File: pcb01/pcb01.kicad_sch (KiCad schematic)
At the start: 26 parts, among them J1 DIN41612_02x32_AC, J2 Conn_01x08_Socket, J3 Conn_01x16_Socket, SW1 SW_Push, U1 W65C02SxP, U2 HM62256BLP, U3 27C512, U4 PAL20RS10, U5 74LS138, U6 74HCT574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

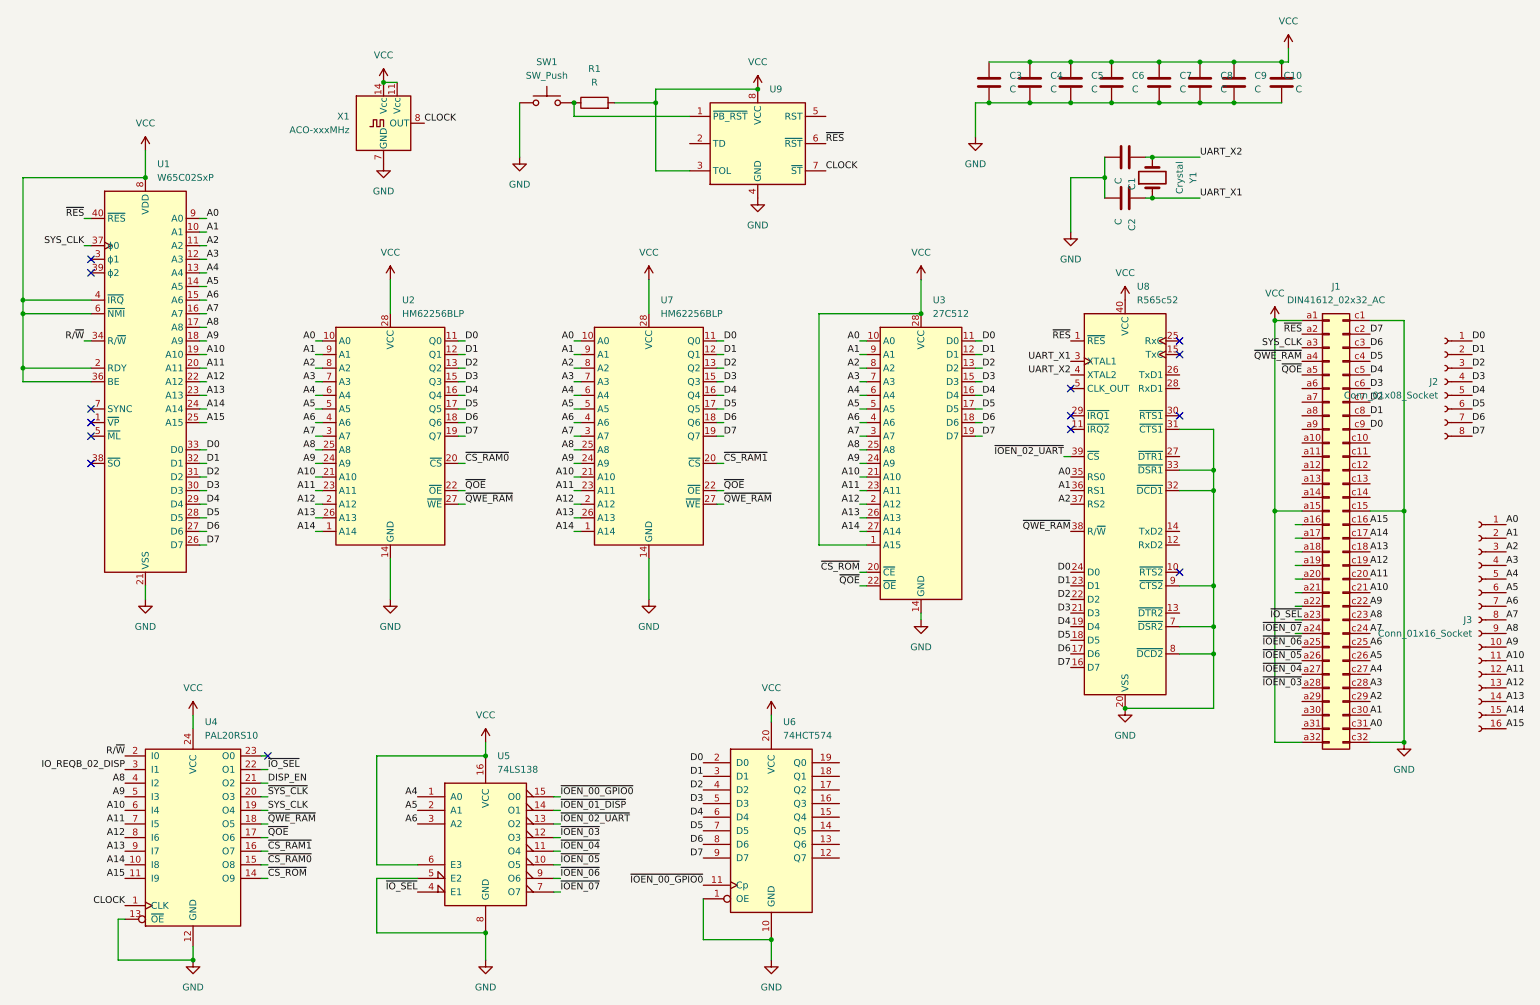
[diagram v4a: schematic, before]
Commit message: fix some schematic bugs
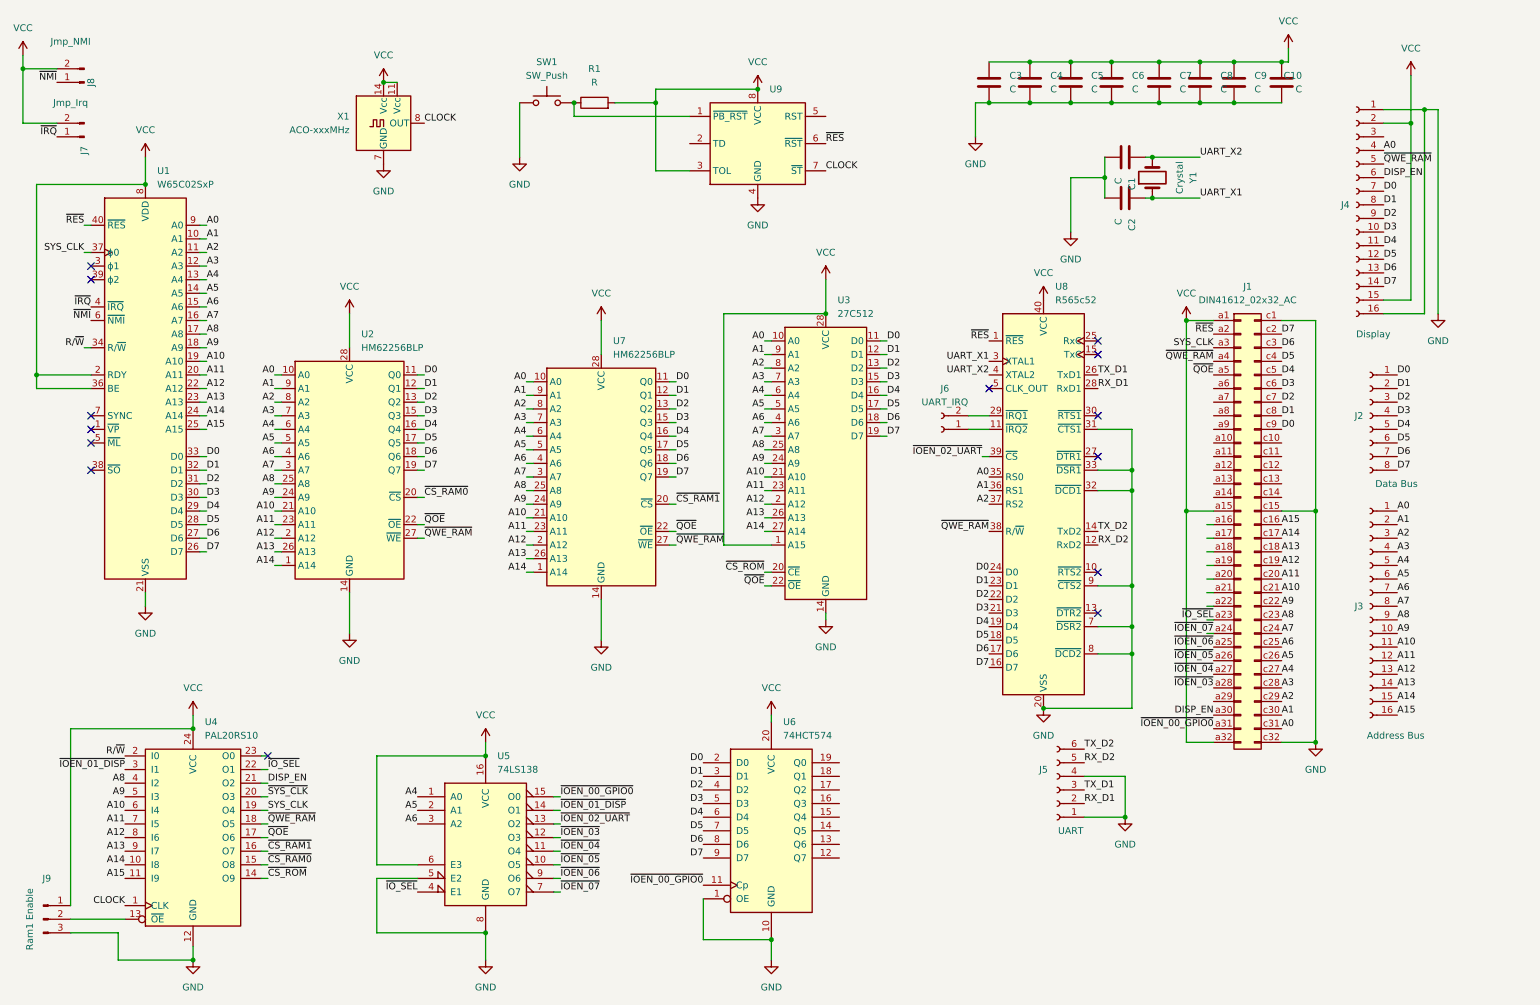
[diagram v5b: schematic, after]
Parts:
- added J4: Display, Connector_PinSocket_2.54mm:PinSocket_1x16_P2.54mm_Vertical, symbol Connector:Conn_01x16_Socket
- added J5: UART, Connector_PinSocket_2.54mm:PinSocket_1x06_P2.54mm_Vertical, symbol Connector:Conn_01x06_Socket
- added J6: UART_IRQ, Connector_PinHeader_2.00mm:PinHeader_1x02_P2.00mm_Vertical, symbol Connector:Conn_01x02_Socket
- added J7: Jmp_Irq, Connector_PinHeader_2.00mm:PinHeader_1x02_P2.00mm_Vertical, symbol Connector:Conn_01x02_Pin
- added J8: Jmp_NMI, Connector_PinHeader_2.00mm:PinHeader_1x02_P2.00mm_Vertical, symbol Connector:Conn_01x02_Pin
- added J9: Ram1 Enable, Connector_PinHeader_2.54mm:PinHeader_1x03_P2.54mm_Vertical, symbol Connector:Conn_01x03_Pin
- J2: value Conn_01x08_Socket -> Data Bus
- J3: value Conn_01x16_Socket -> Address Bus
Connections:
- net IO_REQB_02_DISP is gone; now on net ~{IOEN_01_DISP}: U4.3 (I1)
- net A0: now also J4.4 (Pin_4)
- net D0: now also J4.7 (Pin_7)
- net D1: now also J4.8 (Pin_8)
- net D2: now also J4.9 (Pin_9)
- net D3: now also J4.10 (Pin_10)
- net D4: now also J4.11 (Pin_11)
- net D5: now also J4.12 (Pin_12)
- net D6: now also J4.13 (Pin_13)
- net D7: now also J4.14 (Pin_14)
- net DISP_EN: now also J1.a30 (Pin_a30), J4.6 (Pin_6)
- net GND: now also J4.1 (Pin_1), J4.16 (Pin_16), J5.1 (Pin_1), J5.4 (Pin_4), J9.3 (Pin_3); no longer U4.13 (~{OE})
- net VCC: now also J4.15 (Pin_15), J4.2 (Pin_2), J7.2 (Pin_2), J8.2 (Pin_2), J9.1 (Pin_1); no longer U1.4 (~{IRQ}), U1.6 (~{NMI})
- net ~{IOEN_00_GPIO0}: now also J1.a31 (Pin_a31)
- net ~{QWE_RAM}: now also J4.5 (Pin_5)
- net at U8.11 (~{IRQ2}): now also J6.1 (Pin_1)
- net RX_D2: now reaches U8.12 (RxD2)
- net RX_D2: now also J5.5 (Pin_5)
- net TX_D2: now reaches U8.14 (TxD2)
- net TX_D2: now also J5.6 (Pin_6)
- net TX_D1: now reaches U8.26 (TxD1)
- net TX_D1: now also J5.3 (Pin_3)
- net RX_D1: now reaches U8.28 (RxD1)
- net RX_D1: now also J5.2 (Pin_2)
- net at U8.29 (~{IRQ1}): now also J6.2 (Pin_2)
- new net: J9.2 (Pin_2), U4.13 (~{OE})
- new net ~{IRQ}: J7.1 (Pin_1), U1.4 (~{IRQ})
- new net ~{NMI}: J8.1 (Pin_1), U1.6 (~{NMI})
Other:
- moved on the sheet: J1, J2, J3, U1, U2, U3, U7, U8

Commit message: pcb refinement
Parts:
- added C11: C_Polarized, Capacitor_THT:CP_Radial_D8.0mm_P5.00mm, symbol Device:C_Polarized
- added C12, C13: C_Polarized, Capacitor_THT:CP_Radial_D5.0mm_P2.50mm, symbol Device:C_Polarized
- added J10: Conn_01x02_Socket, Connector_PinSocket_2.54mm:PinSocket_1x02_P2.54mm_Vertical, symbol Connector:Conn_01x02_Socket
- U1, U8: footprint Package_DIP:DIP-40_W15.24mm -> Package_DIP:DIP-40_W15.24mm_Socket
- U3: footprint Package_DIP:DIP-28_W15.24mm -> Package_DIP:DIP-28_W15.24mm_Socket
- U4: footprint Package_DIP:DIP-24_W7.62mm -> Package_DIP:DIP-24_W7.62mm_Socket
- U5: footprint Package_DIP:DIP-16_W7.62mm -> Package_DIP:DIP-16_W7.62mm_Socket
- U6: footprint Package_DIP:DIP-20_W7.62mm -> Package_DIP:DIP-20_W7.62mm_Socket
- U9: value ~ -> MAX1232
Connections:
- net GND: now also C11.2, C12.2, C13.2, J10.2 (Pin_2)
- net VCC: now also C11.1, C12.1, C13.1, J10.1 (Pin_1)
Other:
- moved on the sheet: C10, C3, C4, C5, C6, C7, C8, C9

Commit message: connect GPIO0
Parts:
- added J11: Conn_01x09, Connector_PinSocket_2.54mm:PinSocket_1x09_P2.54mm_Vertical, symbol Connector_Generic:Conn_01x09
- added RV1: R_LCD_BIAS, Potentiometer_THT:Potentiometer_Vishay_T73YP_Vertical, symbol Device:R_Potentiometer_Small
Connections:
- net GND: now also J11.1 (Pin_1), RV1.3
- net VCC: now also RV1.1
- net ~{SYS_CLK}: now also J1.a16 (Pin_a16)
- net LCD_BIAS: now reaches J4.3 (Pin_3)
- net LCD_BIAS: now also RV1.2
- net at U6.12 (Q7): now also J11.9 (Pin_9)
- net at U6.13 (Q6): now also J11.8 (Pin_8)
- net at U6.14 (Q5): now also J11.7 (Pin_7)
- net at U6.15 (Q4): now also J11.6 (Pin_6)
- net at U6.16 (Q3): now also J11.5 (Pin_5)
- net at U6.17 (Q2): now also J11.4 (Pin_4)
- net at U6.18 (Q1): now also J11.3 (Pin_3)
- net at U6.19 (Q0): now also J11.2 (Pin_2)
- no-connect marks 14 -> 37

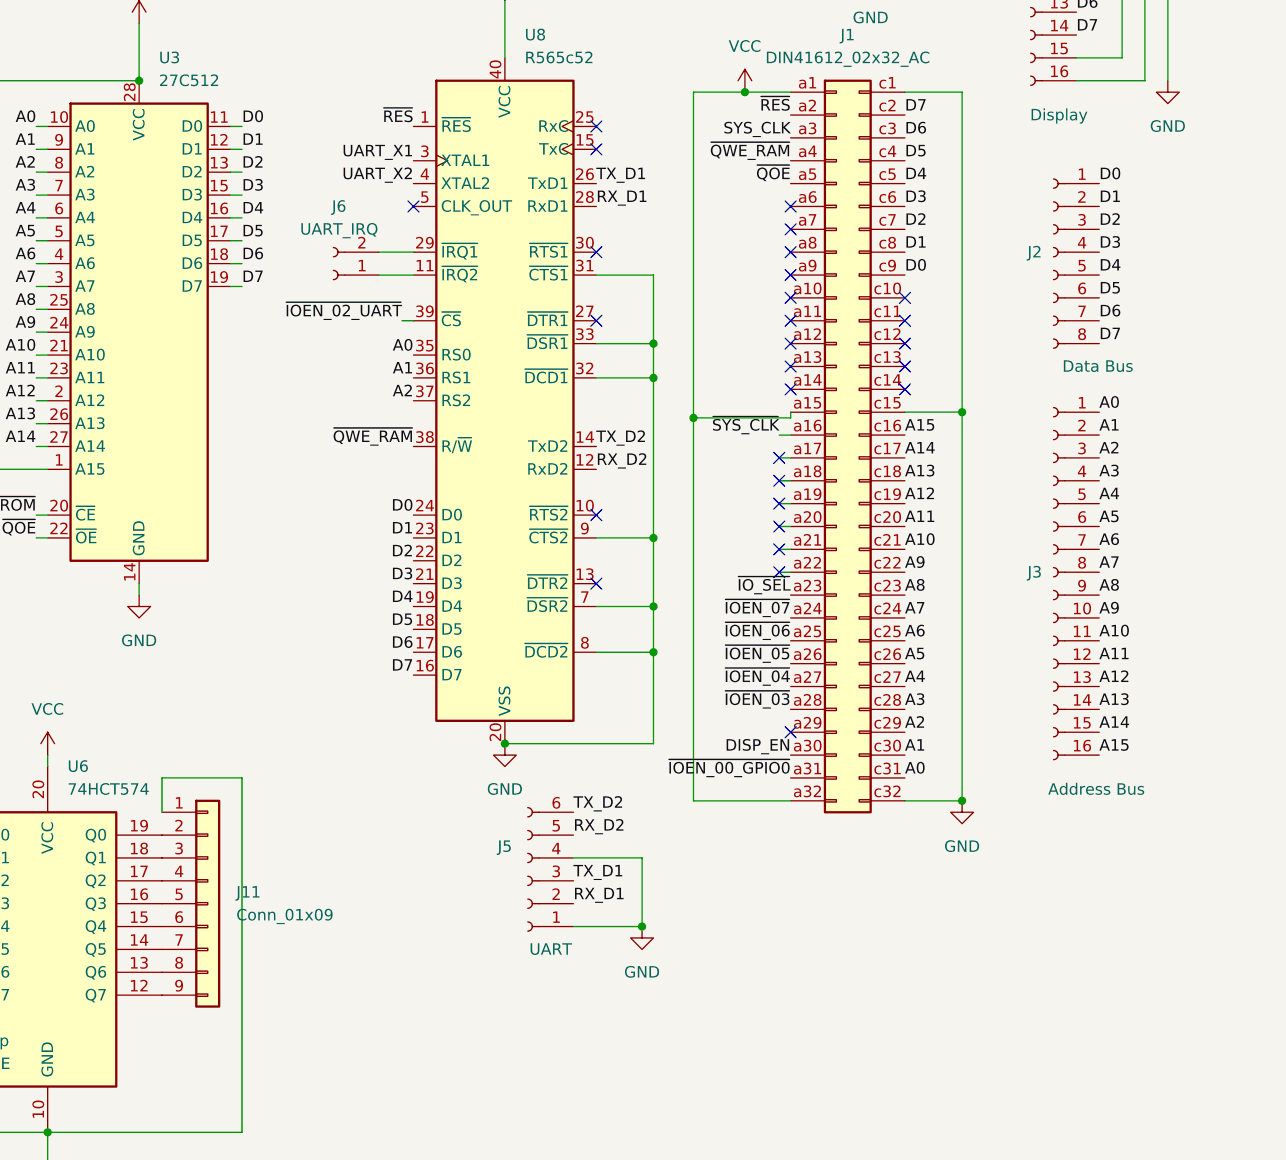
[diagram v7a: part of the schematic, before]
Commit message: add gpio00 leds
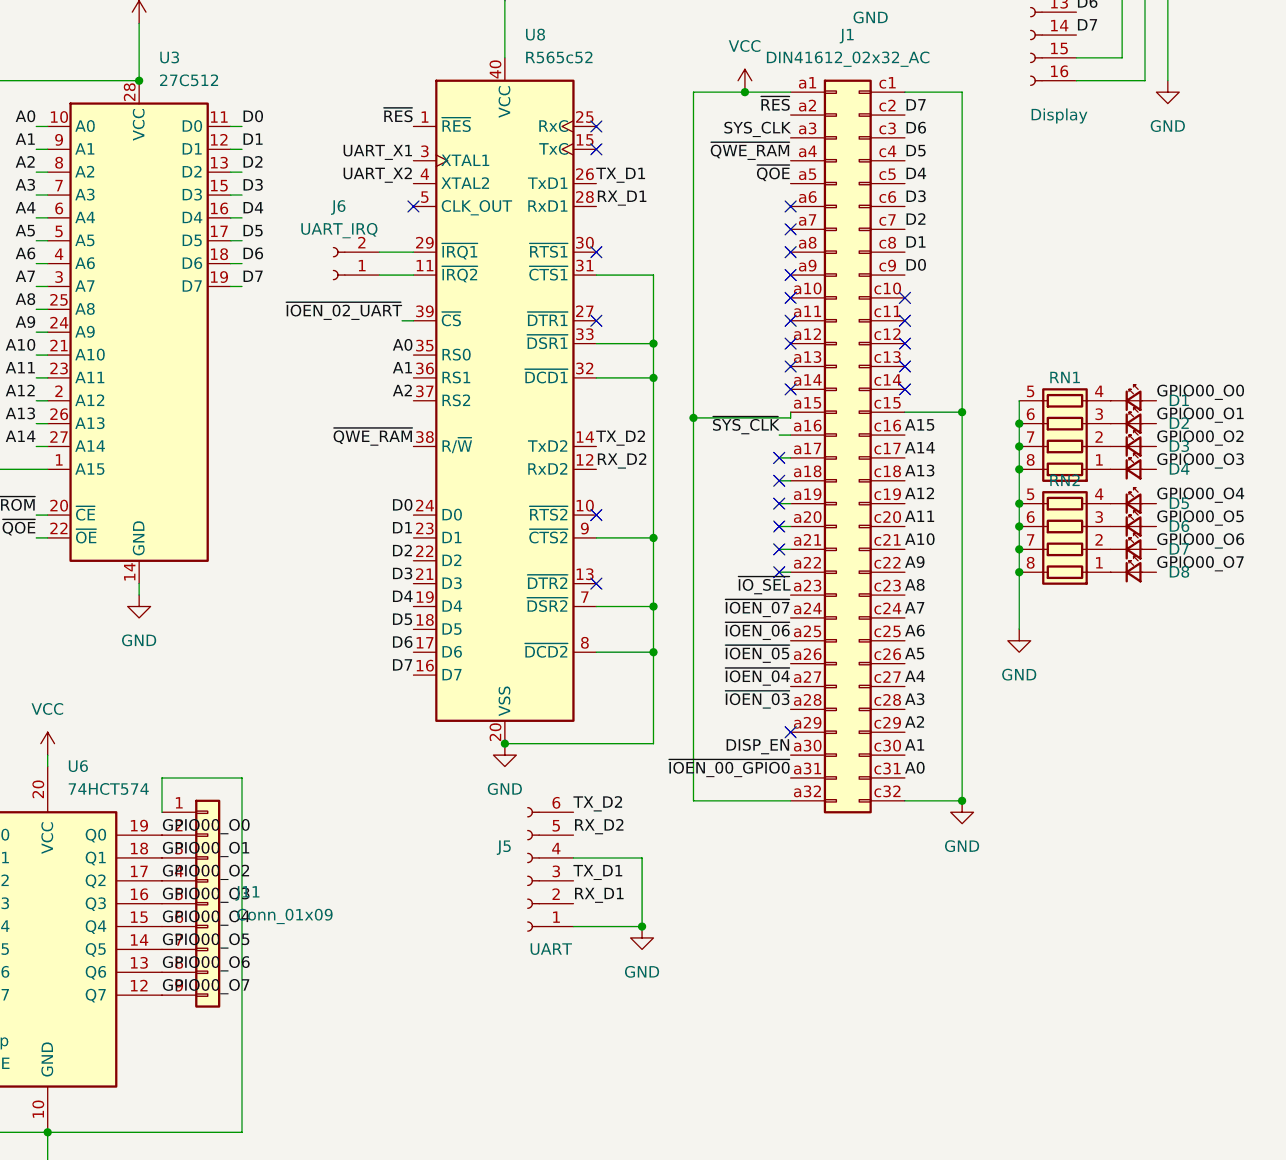
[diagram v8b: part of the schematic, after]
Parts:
- removed J2: Data Bus, Connector_PinSocket_2.54mm:PinSocket_1x08_P2.54mm_Vertical, symbol Connector:Conn_01x08_Socket
- removed J3: Address Bus, Connector_PinSocket_2.54mm:PinSocket_1x16_P2.54mm_Vertical, symbol Connector:Conn_01x16_Socket
- added D1, D2, D3, D4, D5, D6, D7, D8: LED_Small, LED_SMD:LED_1206_3216Metric, symbol Device:LED_Small
- added RN1, RN2: R_Pack04, Resistor_SMD:R_Array_Concave_4x0402, symbol Device:R_Pack04
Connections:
- net GND: now also RN1.5 (R4.2), RN1.6 (R3.2), RN1.7 (R2.2), RN1.8 (R1.2), RN2.5 (R4.2), RN2.6 (R3.2), RN2.7 (R2.2), RN2.8 (R1.2)
- net GPIO00_O0: now reaches J11.2 (Pin_2), U6.19 (Q0)
- net GPIO00_O0: now also D1.2 (A)
- net GPIO00_O1: now reaches J11.3 (Pin_3), U6.18 (Q1)
- net GPIO00_O1: now also D2.2 (A)
- net GPIO00_O2: now reaches J11.4 (Pin_4), U6.17 (Q2)
- net GPIO00_O2: now also D3.2 (A)
- net GPIO00_O3: now reaches J11.5 (Pin_5), U6.16 (Q3)
- net GPIO00_O3: now also D4.2 (A)
- net GPIO00_O4: now reaches J11.6 (Pin_6), U6.15 (Q4)
- net GPIO00_O4: now also D5.2 (A)
- net GPIO00_O5: now reaches J11.7 (Pin_7), U6.14 (Q5)
- net GPIO00_O5: now also D6.2 (A)
- net GPIO00_O6: now reaches J11.8 (Pin_8), U6.13 (Q6)
- net GPIO00_O6: now also D7.2 (A)
- net GPIO00_O7: now reaches J11.9 (Pin_9), U6.12 (Q7)
- net GPIO00_O7: now also D8.2 (A)
- new net: D4.1 (K), RN1.1 (R1.1)
- new net: D6.1 (K), RN2.3 (R3.1)
- new net: D2.1 (K), RN1.3 (R3.1)
- new net: D8.1 (K), RN2.1 (R1.1)
- new net: D7.1 (K), RN2.2 (R2.1)
- new net: D5.1 (K), RN2.4 (R4.1)
- new net: D3.1 (K), RN1.2 (R2.1)
- new net: D1.1 (K), RN1.4 (R4.1)
